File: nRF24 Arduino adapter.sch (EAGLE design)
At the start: 4 parts

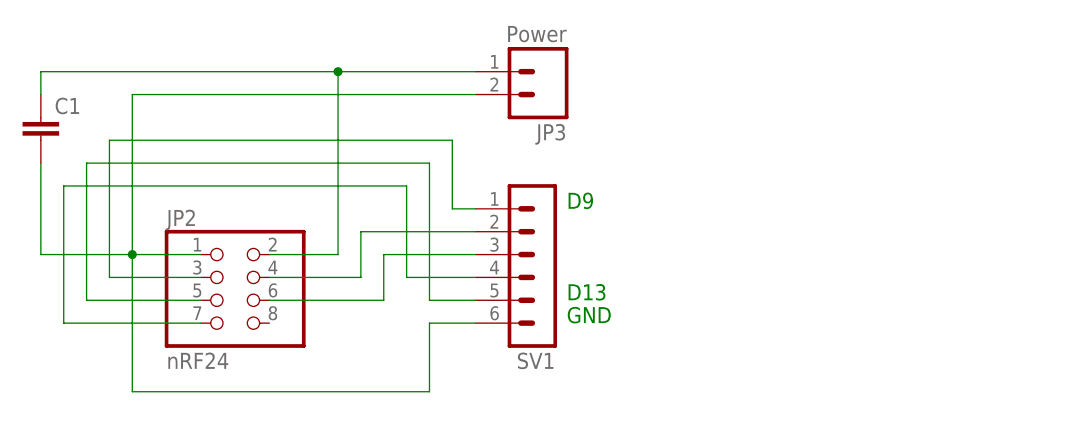
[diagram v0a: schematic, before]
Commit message: New version of schema
Thanks to Rikard "Ornotermes" Lindström for the help
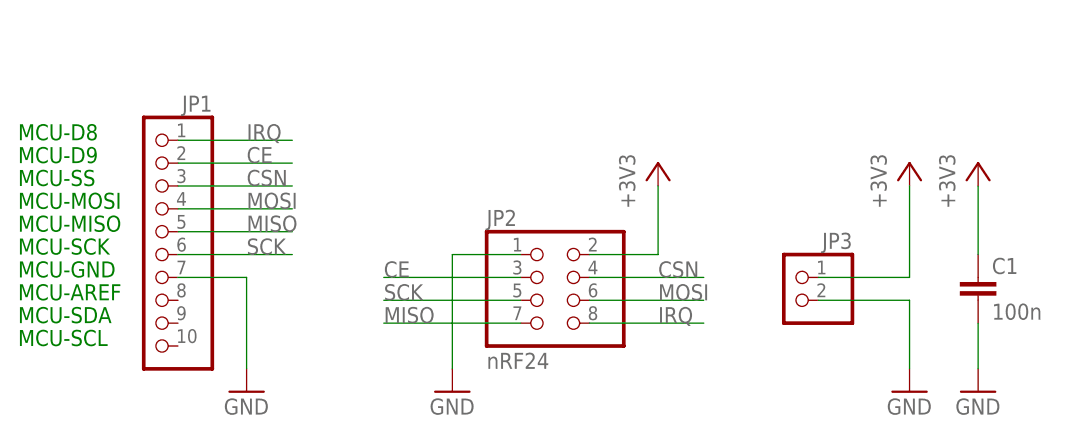
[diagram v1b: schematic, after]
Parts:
- removed SV1: (no value), con-lstb:MA06-1
- added JP1: (no value), pinhead:PINHD-1X10
- C1: value (none) -> 100n; device capacitor-wima:C2,5-3 -> capacitor-wima:C7.5/3
- JP3: value Power -> (none); device SparkFun-Connectors:M02LOCK_LONGPADS -> pinhead:PINHD-1X2
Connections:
- net N$3 renamed +3V3
- removed net N$1: C1.2, JP2.1, JP3.2, SV1.6
- removed net N$2: JP2.3, SV1.1
- removed net N$4: JP2.4, SV1.2
- removed net N$5: JP2.6, SV1.3
- removed net N$6: JP2.5, SV1.5
- removed net N$8: JP2.7, SV1.4
- new net CE: JP1.2, JP2.3
- new net CSN: JP1.3, JP2.4
- new net GND: C1.2, JP1.7, JP2.1, JP3.2
- new net IRQ: JP1.1, JP2.8
- new net MISO: JP1.5, JP2.7
- new net MOSI: JP1.4, JP2.6
- new net SCK: JP1.6, JP2.5
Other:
- note added: "MCU-AREF"
- note added: "MCU-D8"
- note added: "MCU-D9"
- note added: "MCU-GND"
- note added: "MCU-MISO"
- note added: "MCU-MOSI"
- note added: "MCU-SCK"
- note added: "MCU-SCL"
- note added: "MCU-SDA"
- note added: "MCU-SS"
- note removed: "D13"
- note removed: "D9"
- note removed: "GND"
- moved on the sheet: C1, JP2, JP3
